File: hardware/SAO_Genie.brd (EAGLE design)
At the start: 49.9 x 25.4 mm, 24 parts, among them J1 CONN_02X2_NO_SILK, J2 SAO OUT, U4 ATSAMD21G-A, Y1 32.768KHZ

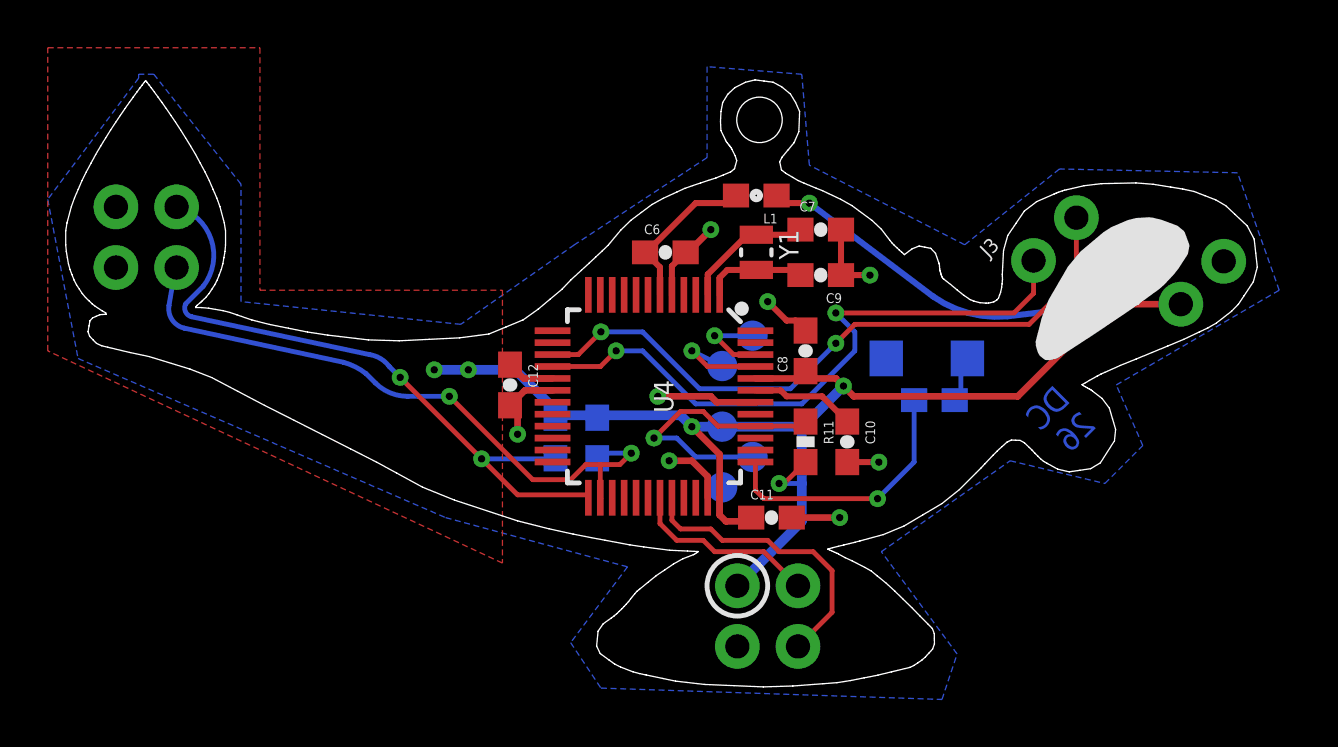
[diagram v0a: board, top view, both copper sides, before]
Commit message: update hardware schematic, board layout, and bill of material
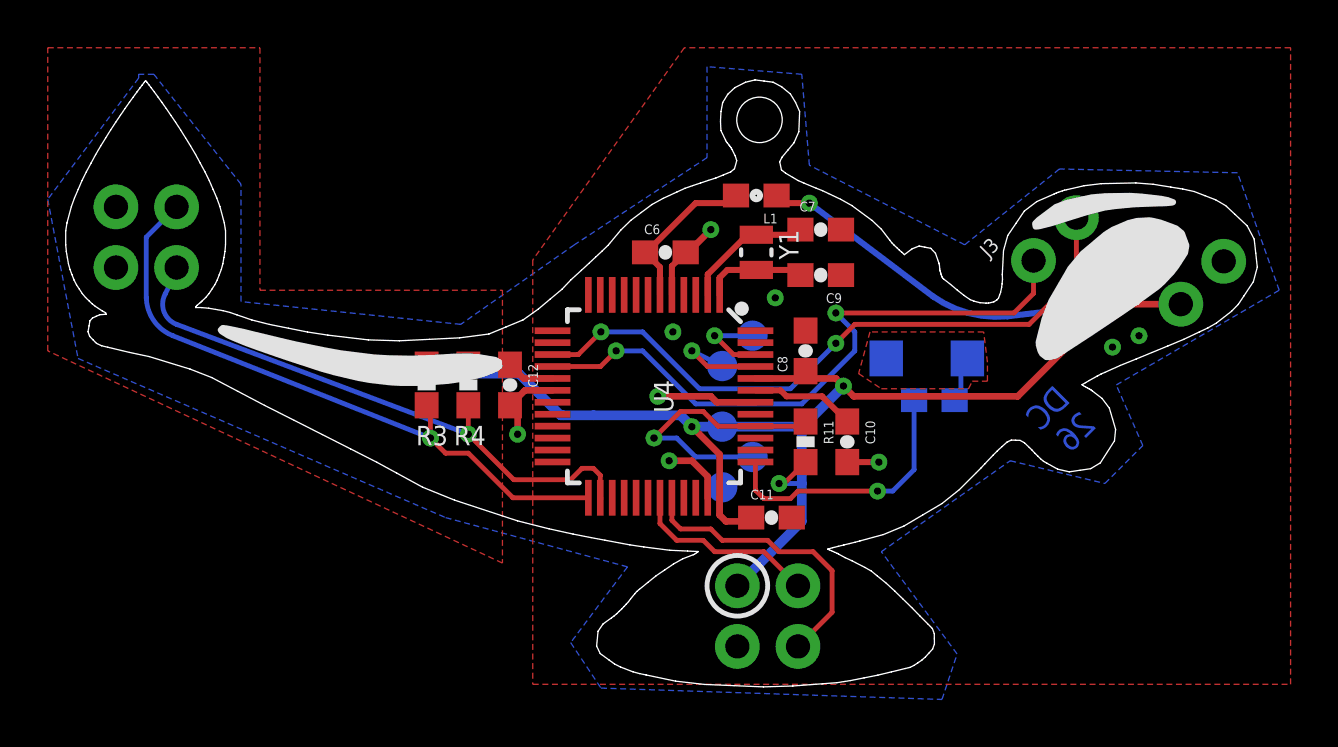
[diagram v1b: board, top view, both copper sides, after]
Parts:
- added FRAME1: FRAME-LETTER-BLANKNO_PACKAGE, SparkFun-Aesthetics:DUMMY
- R5: value 150 -> 68
- moved R4 5.84 mm to (30.3, 12.5), flipped to the top
- moved R3 5.84 mm to (28.6, 12.5), flipped to the top
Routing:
- net 3.3V: track 73.3 -> 80.6 mm
- net GND: track 22.4 -> 15.2 mm, vias 8 -> 9
- net SCL_OUT: track 27.0 -> 24.5 mm, vias 2 -> 1
- net SDA_OUT: track 27.5 -> 27.0 mm, vias 2 -> 1
- added copper zone on layer 1, net GND
- added copper zone on layer 1, net N$1
